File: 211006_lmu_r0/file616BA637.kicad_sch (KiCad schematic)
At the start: 13 parts, among them U2 ISO1042DWVR

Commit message: Updated lmu project with relative library paths and fixed broken symbols
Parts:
- L2: symbol Device:L_Core_Ferrite_Coupled -> Device:L_Ferrite_Coupled
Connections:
- net +5V: now also U2.8 (VCC2)
- net CAN_RX: now also U2.2 (RXD)
- net CAN_S: now also U2.5 (GND2)
- net CAN_TX: now also U2.3 (TXD)
- net GND: now also C13.2, U2.4 (GND1)
- net at C11.1, D5.1 (K), L2.4: now also U2.6 (CANL)
- net at C10.1, D5.2 (K), L2.2: now also U2.7 (CANH)
- net +3V3: now reaches C13.1
- net +3V3: now also U2.1 (VCC1)
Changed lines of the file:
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@@
       (effects (font (size 1.27 1.27)) hide)
     )
+    (pin "1")
+    (pin "2")
+    (pin "3")
+    (pin "4")
+    (pin "5")
+    (pin "6")
+    (pin "7")
+    (pin "8")
   )
   (symbol (lib_id "+3v3_iso:+3V3_ISO") (at 199.39 90.17 0) (unit 1)
@@
       (effects (font (size 1.27 1.27)) hide)
     )
+    (pin "1")
   )
   (symbol (lib_id "power:+5V") (at 161.29 90.17 0) (unit 1)
@@
       (effects (font (size 1.27 1.27)) hide)
     )
+    (pin "1")
   )
   (symbol (lib_id "power:GND") (at 166.37 111.76 0) (unit 1)
@@
     (pin "2")
   )
-  (symbol (lib_id "Device:L_Core_Ferrite_Coupled") (at 95.25 93.98 0) (unit 1)
+  (symbol (lib_id "Device:L_Ferrite_Coupled") (at 95.25 93.98 0) (unit 1)
     (in_bom yes) (on_board yes)
     (property "Reference" "L2" (id 0) (at 95.25 86.8426 0))

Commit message: Updated some components to make sourcing easier
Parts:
- C10, C11, C12, C13, C7, C8, C9, R3, R4, R5: Manufacturer (none) -> -; Part Number (none) -> -
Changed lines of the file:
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@@
+      (effects (font (size 1.27 1.27)) hide)
+    )
+    (property "Part Number" "-" (id 4) (at 158.75 110.49 0)
+      (effects (font (size 1.27 1.27)) hide)
+    )
+    (property "Manufacturer" "-" (id 5) (at 158.75 110.49 0)
       (effects (font (size 1.27 1.27)) hide)
     )
@@
     )
     (property "Datasheet" "~" (id 3) (at 152.4 82.55 0)
+      (effects (font (size 1.27 1.27)) hide)
+    )
+    (property "Part Number" "-" (id 4) (at 152.4 82.55 0)
+      (effects (font (size 1.27 1.27)) hide)
+    )
+    (property "Manufacturer" "-" (id 5) (at 152.4 82.55 0)
       (effects (font (size 1.27 1.27)) hide)
     )
@@
     )
     (property "Datasheet" "~" (id 3) (at 55.88 88.9 0)
+      (effects (font (size 1.27 1.27)) hide)
+    )
+    (property "Part Number" "-" (id 4) (at 55.88 88.9 0)
+      (effects (font (size 1.27 1.27)) hide)
+    )
+    (property "Manufacturer" "-" (id 5) (at 55.88 88.9 0)
       (effects (font (size 1.27 1.27)) hide)
     )
@@
       (effects (font (size 1.27 1.27)) hide)
     )
+    (property "Part Number" "-" (id 4) (at 62.23 93.98 0)
+      (effects (font (size 1.27 1.27)) hide)
+    )
+    (property "Manufacturer" "-" (id 5) (at 62.23 93.98 0)
+      (effects (font (size 1.27 1.27)) hide)
+    )
     (pin "1")
     (pin "2")
@@
       (effects (font (size 1.27 1.27)) hide)
     )
+    (property "Part Number" "-" (id 4) (at 82.55 102.87 0)
+      (effects (font (size 1.27 1.27)) hide)
+    )
+    (property "Manufacturer" "-" (id 5) (at 82.55 102.87 0)
+      (effects (font (size 1.27 1.27)) hide)
+    )
     (pin "1")
     (pin "2")
@@
       (effects (font (size 1.27 1.27)) hide)
     )
+    (property "Part Number" "-" (id 4) (at 88.9 102.87 0)
+      (effects (font (size 1.27 1.27)) hide)
+    )
+    (property "Manufacturer" "-" (id 5) (at 88.9 102.87 0)
+      (effects (font (size 1.27 1.27)) hide)
+    )
     (pin "1")
     (pin "2")
@@
       (effects (font (size 1.27 1.27)) hide)
     )
+    (property "Part Number" "-" (id 4) (at 104.14 102.87 0)
+      (effects (font (size 1.27 1.27)) hide)
+    )
+    (property "Manufacturer" "-" (id 5) (at 104.14 102.87 0)
+      (effects (font (size 1.27 1.27)) hide)
+    )
     (pin "1")
     (pin "2")
@@
       (effects (font (size 1.27 1.27)) hide)
     )
+    (property "Part Number" "-" (id 4) (at 110.49 102.87 0)
+      (effects (font (size 1.27 1.27)) hide)
+    )
+    (property "Manufacturer" "-" (id 5) (at 110.49 102.87 0)
+      (effects (font (size 1.27 1.27)) hide)
+    )
     (pin "1")
     (pin "2")
@@
       (effects (font (size 1.27 1.27)) hide)
     )
+    (property "Part Number" "-" (id 4) (at 55.88 99.06 0)
+      (effects (font (size 1.27 1.27)) hide)
+    )
+    (property "Manufacturer" "-" (id 5) (at 55.88 99.06 0)
+      (effects (font (size 1.27 1.27)) hide)
+    )
     (pin "1")
     (pin "2")
@@
       (effects (font (size 1.27 1.27)) hide)
     )
+    (property "Part Number" "-" (id 4) (at 199.39 93.98 0)
+      (effects (font (size 1.27 1.27)) hide)
+    )
+    (property "Manufacturer" "-" (id 5) (at 199.39 93.98 0)
+      (effects (font (size 1.27 1.27)) hide)
+    )

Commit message: fixed footprints for headers, started planning out zones
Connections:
- net CAN_L: now also L2.4; no longer L2.3
- net GND: no longer C13.2, U2.4 (GND1)
- net at C11.1, D5.1 (K), U2.6 (CANL): now also L2.3; no longer L2.4
- net +3V3 renamed +3V3_ISO
- new net GND_ISO: C13.2, U2.4 (GND1)

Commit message: updated pcb still need to find j11
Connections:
- net CAN_PRE_N: now reaches C11.1, D5.1 (K), L2.3, U2.6 (CANL)
- net CAN_PRE_P: now reaches C10.1, D5.2 (K), L2.2, U2.7 (CANH)
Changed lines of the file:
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@@
+    (effects (font (size 1.27 1.27)) (justify left bottom))
+  )
+  (label "CAN_PRE_P" (at 130.81 90.17 0)
+    (effects (font (size 1.27 1.27)) (justify left bottom))
+  )
+  (label "CAN_PRE_N" (at 130.81 97.79 0)
     (effects (font (size 1.27 1.27)) (justify left bottom))
   )

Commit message: fixed issues on higher cells, study into how to route
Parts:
- U2: footprint SOIC127P1150X280-8N -> ISO1042DWVR:SOIC127P1150X280-8N
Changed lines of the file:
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@@
     (property "Reference" "U2" (id 0) (at 175.26 83.3882 0))
     (property "Value" "ISO1042DWVR" (id 1) (at 175.26 85.6996 0))
-    (property "Footprint" "SOIC127P1150X280-8N" (id 2) (at 167.64 105.41 0)
+    (property "Footprint" "ISO1042DWVR:SOIC127P1150X280-8N" (id 2) (at 167.64 105.41 0)
       (effects (font (size 1.27 1.27)) (justify left bottom) hide)
     )

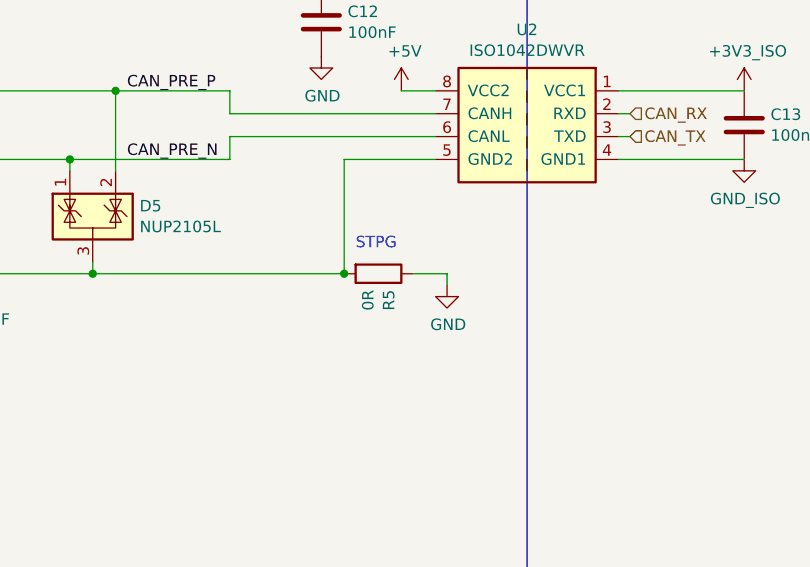
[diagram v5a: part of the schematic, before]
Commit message: Routed vehicle section
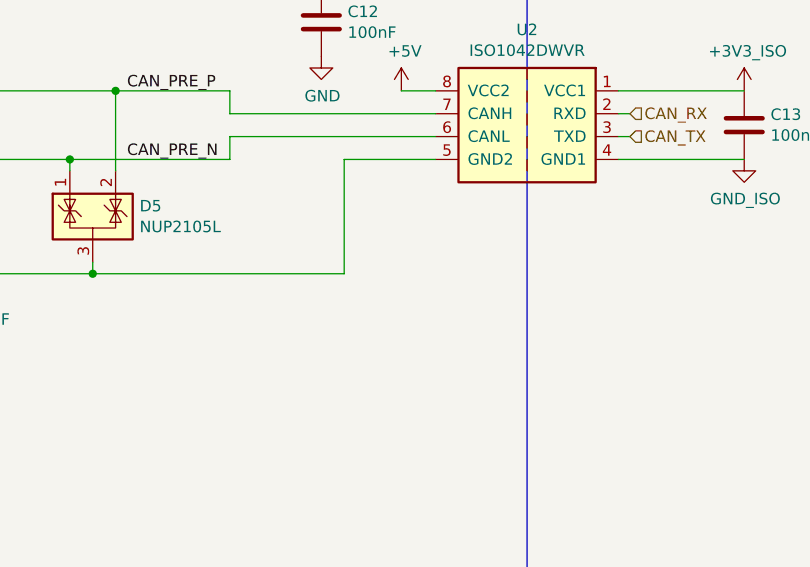
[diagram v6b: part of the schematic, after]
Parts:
- removed R5: 0R, Resistor_SMD:R_0805_2012Metric_Pad1.20x1.40mm_HandSolder, symbol Device:R
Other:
- note removed: "STPG"
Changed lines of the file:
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@@
   (junction (at 104.14 90.17) (diameter 0) (color 0 0 0 0)
   )
-  (junction (at 154.94 110.49) (diameter 0) (color 0 0 0 0)
-  )
   (junction (at 127 110.49) (diameter 0) (color 0 0 0 0)
   )
@@
     (stroke (width 0) (type default) (color 0 0 0 0))
   )
-  (wire (pts (xy 166.37 110.49) (xy 166.37 111.76))
-    (stroke (width 0) (type default) (color 0 0 0 0))
-  )
   (wire (pts (xy 88.9 97.79) (xy 67.31 97.79))
     (stroke (width 0) (type default) (color 0 0 0 0))
@@
     (stroke (width 0) (type default) (color 0 0 0 0))
   )
-  (wire (pts (xy 162.56 110.49) (xy 166.37 110.49))
-    (stroke (width 0) (type default) (color 0 0 0 0))
-  )
   (wire (pts (xy 82.55 90.17) (xy 90.17 90.17))
     (stroke (width 0) (type default) (color 0 0 0 0))
@@
   (wire (pts (xy 67.31 102.87) (xy 67.31 97.79))
     (stroke (width 0) (type default) (color 0 0 0 0))
-  )
-  (text "STPG" (at 156.21 107.95 0)
-    (effects (font (size 1.27 1.27)) (justify left bottom))
   )
   (label "CAN_PRE_P" (at 130.81 90.17 0)
@@
     (pin "1")
   )
-  (symbol (lib_id "power:GND") (at 166.37 111.76 0) (unit 1)
-    (in_bom yes) (on_board yes)
-    (property "Reference" "#PWR013" (id 0) (at 166.37 118.11 0)
-      (effects (font (size 1.27 1.27)) hide)
-    )
-    (property "Value" "GND" (id 1) (at 166.497 116.1542 0))
-    (property "Footprint" "" (id 2) (at 166.37 111.76 0)
-      (effects (font (size 1.27 1.27)) hide)
-    )
-    (property "Datasheet" "" (id 3) (at 166.37 111.76 0)
-      (effects (font (size 1.27 1.27)) hide)
-    )
-    (pin "1")
-  )
-  (symbol (lib_id "Device:R") (at 158.75 110.49 270) (unit 1)
-    (in_bom yes) (on_board yes)
-    (property "Reference" "R5" (id 0) (at 159.9184 112.268 0)
-      (effects (font (size 1.27 1.27)) (justify left))
-    )
-    (property "Value" "0R" (id 1) (at 157.607 112.268 0)
-      (effects (font (size 1.27 1.27)) (justify left))
-    )
-    (property "Footprint" "Resistor_SMD:R_0805_2012Metric_Pad1.20x1.40mm_HandSolder" (id 2) (at 158.75 108.712 90)
-      (effects (font (size 1.27 1.27)) hide)
-    )
-    (property "Datasheet" "~" (id 3) (at 158.75 110.49 0)
-      (effects (font (size 1.27 1.27)) hide)
-    )
-    (property "Part Number" "-" (id 4) (at 158.75 110.49 0)
-      (effects (font (size 1.27 1.27)) hide)
-    )
-    (property "Manufacturer" "-" (id 5) (at 158.75 110.49 0)
-      (effects (font (size 1.27 1.27)) hide)
-    )
-    (pin "1")
-    (pin "2")
-  )
   (symbol (lib_id "Device:C") (at 152.4 82.55 0) (unit 1)
